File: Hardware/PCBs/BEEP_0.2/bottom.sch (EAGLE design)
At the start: 35 parts, among them IC1 74HCT00D, IC2 TCS32X0, Q2 IRLML2244, Q5 IRLML2244, Q6 IRLML2244, Q8 IRLML2244

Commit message: add simulation for comperator with hysteresis add library with atmel products (by element14) continue work on bottom shematic
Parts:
- removed 5V, GND, I1, I2, I3, I4, O1, O2, O3, O4: PTR1TP11SQ, testpad:PTR1TP11SQ
- removed LED1, LED2, LED3: (no value), led:LED3MM
- added C2, C3: 100n, rcl:C-EUC0805
- added D1, D2, D3, D4: CNY70, BEEP:CNY70
- added D5: (no value), diode:ZENER-DIODESMB
- added IC3, IC4: TCS32X0, BEEP:TCS32X0
- added Q1: DMN2075U, BEEP:DMN2075U
- added R12, R13, R14, R15, R16, R17, R18, R19, R20, R21, R22, R23, R24, R25, R26, R27, R28, R29, R30, R31, R32, R33, R34, R35, R36: (no value), rcl:R-EU_M0805
- added S1: (no value), switch-omron:40-XX
- added U1: LM239AMDREP, Texas Instruments_By_element14_Batch_1:LM239AMDREP
- added U2: ATTINY10-TSHR, Atmel_By_element14_Batch_1:ATTINY10-TSHR
- JP1: device pinhead:PINHD-2X5 -> pinhead:PINHD-2X3
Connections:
- removed net GND1: C1.1, IC2.GND, JP1.10, JP1.2, LED1.C, LED2.C, LED3.C, LED4.C, LED5.C, LED6.C
- removed net N$10: I3.TP, IC1C.I0, IC1C.I1
- removed net N$11: I4.TP, IC1D.I0, IC1D.I1
- removed net N$12: O4.TP, R8.2
- removed net N$16: O1.TP, R5.2
- removed net N$20: IC2.S0, JP1.8
- removed net N$21: IC2.S3, JP1.7
- removed net N$22: IC2.NOE, JP1.4
- removed net N$23: IC2.S1, JP1.6
- removed net N$24: C1.2, IC2.VDD, JP1.1
- removed net N$25: IC2.OUT, JP1.3
- removed net N$26: IC2.S2, JP1.5
- removed net N$27: JP1.9, R10.2, R11.2, R9.2
- removed net N$6: O2.TP, R6.2
- removed net N$7: I1.TP, IC1A.I0, IC1A.I1
- removed net N$8: I2.TP, IC1B.I0, IC1B.I1
- removed net N$9: O3.TP, R7.2
- new net +3V3: C1.2, C2.2, C3.2, D1.LED_A, D2.LED_A, D3.LED_A, D4.LED_A, IC2.S0, IC2.S1, IC2.VDD, IC3.S0, IC3.S1, IC3.VDD, IC4.S0, IC4.S1, IC4.VDD, R20.2, R21.2, R22.2, R23.2, R24.2, U1.VCC
- new net +7V: D5.C, R35.2
- new net BATT_GND: JP1.6, Q1.D, S1.S, S1.S1, U2.GND
- new net COLOR_1_NOE: IC2.NOE
- new net COLOR_2_NOE: IC3.NOE
- new net COLOR_3_NOE: IC4.NOE
- new net COMM_COLOR_F_OUT: IC2.OUT, IC3.OUT, IC4.OUT
- new net COMM_COLOR_S2: IC2.S2, IC3.S2, IC4.S2
- new net COMM_COLOR_S3: IC2.S3, IC3.S3, IC4.S3
- new net ENC_L1: R20.1, R30.1, U1.1OUT
- new net ENC_L1_RAW: D1.T_E, R13.2, R26.2
- new net ENC_L2: R21.1, R31.1, U1.2OUT
- new net ENC_L2_RAW: D2.T_E, R15.2, R27.2
- new net ENC_R1: R22.1, R32.1, U1.OUT3
- new net ENC_R1_RAW: D3.T_E, R17.2, R28.2
- new net ENC_R2: R23.1, R33.1, U1.OUT4
- new net ENC_R2_RAW: D4.T_E, R19.2, R29.2
- new net N$43: D1.LED_C, R12.2
- new net N$44: R26.1, R30.2, U1.1IN+
- new net N$45: R27.1, R31.2, U1.2IN+
- new net N$46: D2.LED_C, R14.2
- new net N$47: R28.1, R32.2, U1.3IN+
- new net N$48: D3.LED_C, R16.2
- new net N$49: R29.1, R33.2, U1.4IN+
- new net N$50: D4.LED_C, R18.2
- new net PWM_IN1: IC1A.I0, IC1A.I1
- new net PWM_IN2: IC1B.I0, IC1B.I1
- new net PWM_IN3: IC1C.I0, IC1C.I1
- new net PWM_IN4: IC1D.I0, IC1D.I1
- new net PWM_OUT1: R5.2
- new net PWM_OUT2: R6.2
- new net PWM_OUT3: R7.2
- new net PWM_OUT4: R8.2
- new net RESET: JP1.5, R36.1, U2.PB3
- new net SWITCHED_GROUND: Q1.S
- new net TINY_VCC: D5.A, JP1.2, R36.2, U2.VCC
- new net TPICLK: JP1.3, R34.2, R35.1, S1.P, S1.P1, U2.PB1, U2.PB2
- new net TPIDATA: JP1.1, Q1.G, U2.PB0
- new net U_REF: R24.1, R25.2, U1.1IN-, U1.2IN-, U1.3IN-, U1.4IN-
- net +5V: now also D1.T_C, D2.T_C, D3.T_C, D4.T_C, R10.2, R11.2, R9.2; no longer 5V.TP
- net GND: now also C1.1, C2.1, C3.1, IC1P.GND, IC2.GND, IC3.GND, IC4.GND, LED4.C, LED5.C, LED6.C, R12.1, R13.1, R14.1, R15.1, R16.1, R17.1, R18.1, R19.1, R25.1, R34.1, U1.GND; no longer GND.TP
- net N$17: no longer LED2.A
- net N$18: no longer LED1.A
- net N$19: no longer LED3.A
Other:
- moved on the sheet: C1, IC2, LED4, LED5, LED6, R10, R11, R9

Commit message: add more distance boards continue work on bottom pcb
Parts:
- added JP2: (no value), pinhead:PINHD-1X5
- added JP3: (no value), pinhead:PINHD-2X4
- added JP4: (no value), pinhead:PINHD-1X3
- added X1: (no value), con-ftop-orientation-hole:FTOP-10
- S1: device switch-omron:40-XX -> switch-omron:10-XX
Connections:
- removed net COLOR_1_NOE: IC2.NOE
- removed net COLOR_2_NOE: IC3.NOE
- removed net COLOR_3_NOE: IC4.NOE
- removed net COMM_COLOR_F_OUT: IC2.OUT, IC3.OUT, IC4.OUT
- removed net COMM_COLOR_S2: IC2.S2, IC3.S2, IC4.S2
- removed net COMM_COLOR_S3: IC2.S3, IC3.S3, IC4.S3
- removed net SWITCHED_GROUND: Q1.S
- new net COLOR_DIODE_1: IC2.S2, IC3.S2, IC4.S2, X1-4.1
- new net COLOR_DIODE_2: IC2.S3, IC3.S3, IC4.S3, X1-3.1
- new net COLOR_FREQ_OUT: IC2.OUT, IC3.OUT, IC4.OUT, X1-7.1
- new net COLOR_SENSOR_1: IC2.NOE, X1-2.1
- new net COLOR_SENSOR_2: IC3.NOE, X1-6.1
- new net COLOR_SENSOR_3: IC4.NOE, X1-5.1
- new net COLOR_SENSOR_PWM_LED: R10.2, R11.2, R9.2, X1-9.1
- new net N$6: S1.P, S1.P1, U2.PB2
- new net SWITCHED_GND: JP4.2, Q1.S
- net +3V3: now also X1-10.1
- net +5V: now also JP2.5; no longer R10.2, R11.2, R9.2
- net +7V: now also JP4.3
- net BATT_GND: now also JP4.1
- net ENC_L1: now also JP2.1
- net ENC_L2: now also JP2.2
- net ENC_R1: now also JP2.3
- net ENC_R2: now also JP2.4
- net GND: now also X1-8.1
- net PWM_IN1: now also JP3.1
- net PWM_IN2: now also JP3.3
- net PWM_IN3: now also JP3.5
- net PWM_IN4: now also JP3.7
- net PWM_OUT1: now also JP3.2
- net PWM_OUT2: now also JP3.4
- net PWM_OUT3: now also JP3.6
- net PWM_OUT4: now also JP3.8
- net TPICLK: no longer S1.P, S1.P1, U2.PB2
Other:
- moved on the sheet: R20, R21, R22, R23

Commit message: continue work on bottom pcb
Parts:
- R12: device rcl:R-EU_M0805 -> rcl:R-EU_R0805
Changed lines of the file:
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@@
 <part name="D1" library="BEEP" deviceset="CNY70" device=""/>
 <part name="GND6" library="supply1" deviceset="GND" device=""/>
-<part name="R12" library="rcl" deviceset="R-EU_" device="M0805"/>
+<part name="R12" library="rcl" deviceset="R-EU_" device="R0805"/>
 <part name="R13" library="rcl" deviceset="R-EU_" device="M0805"/>
 <part name="GND7" library="supply1" deviceset="GND" device=""/>

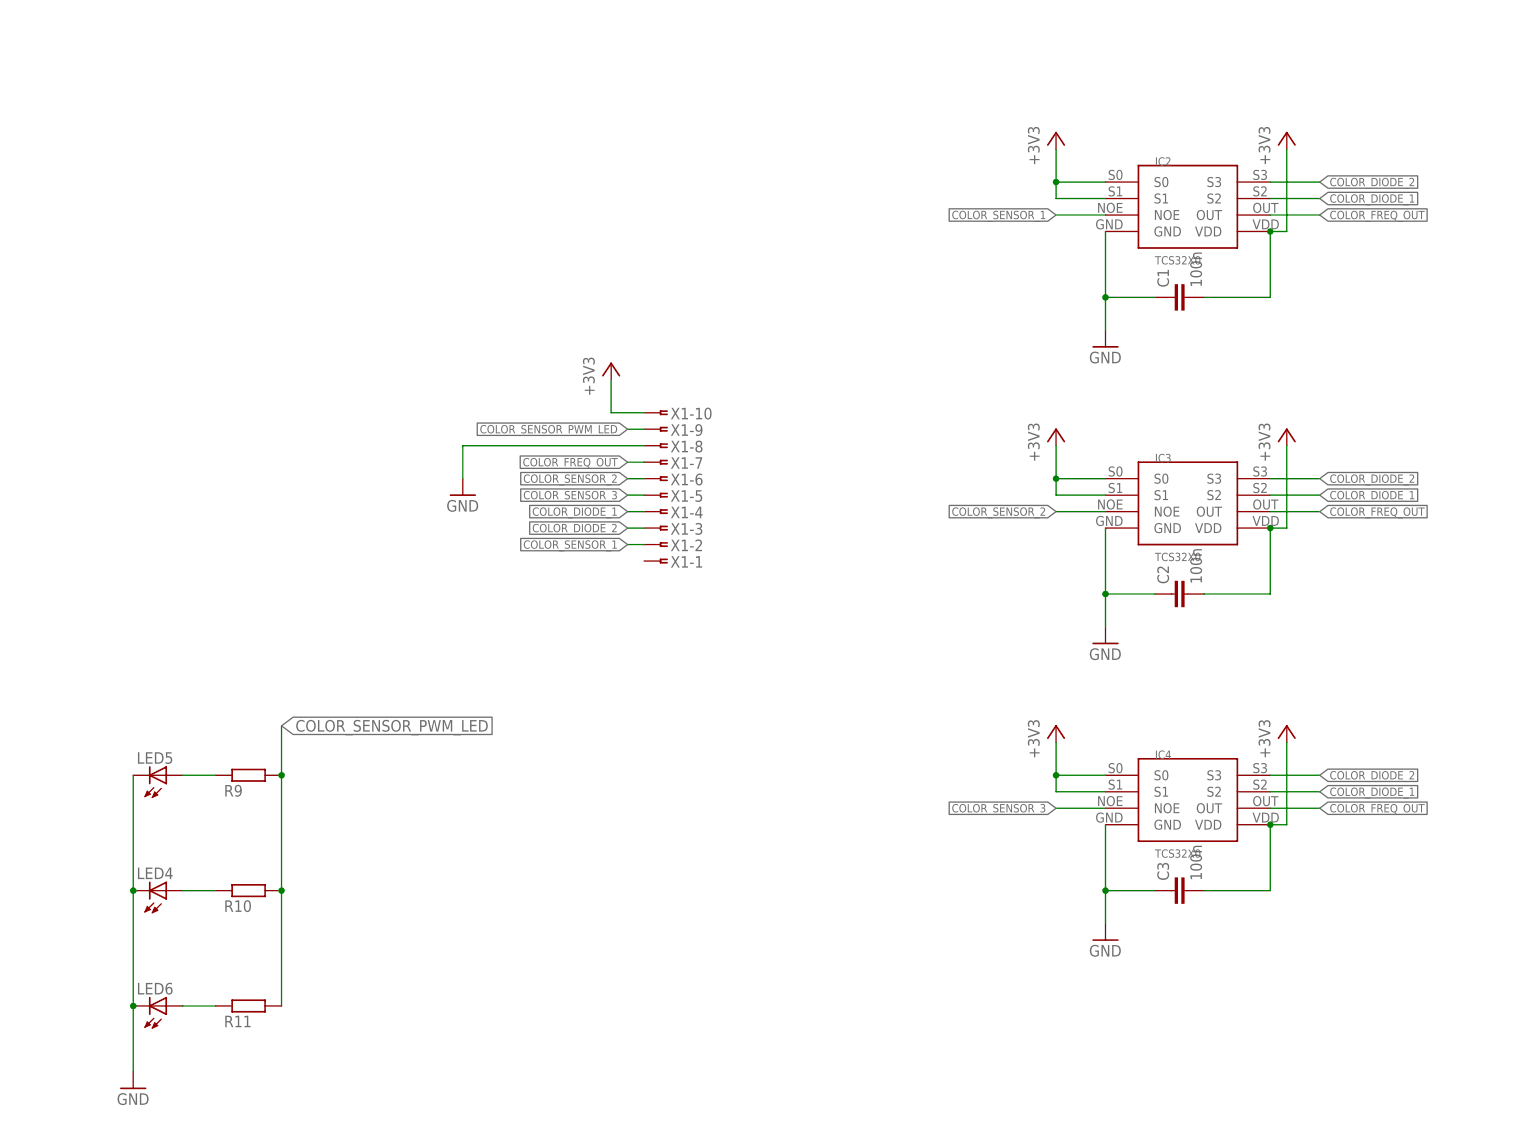
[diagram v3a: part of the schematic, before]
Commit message: continue work on bottom pcb
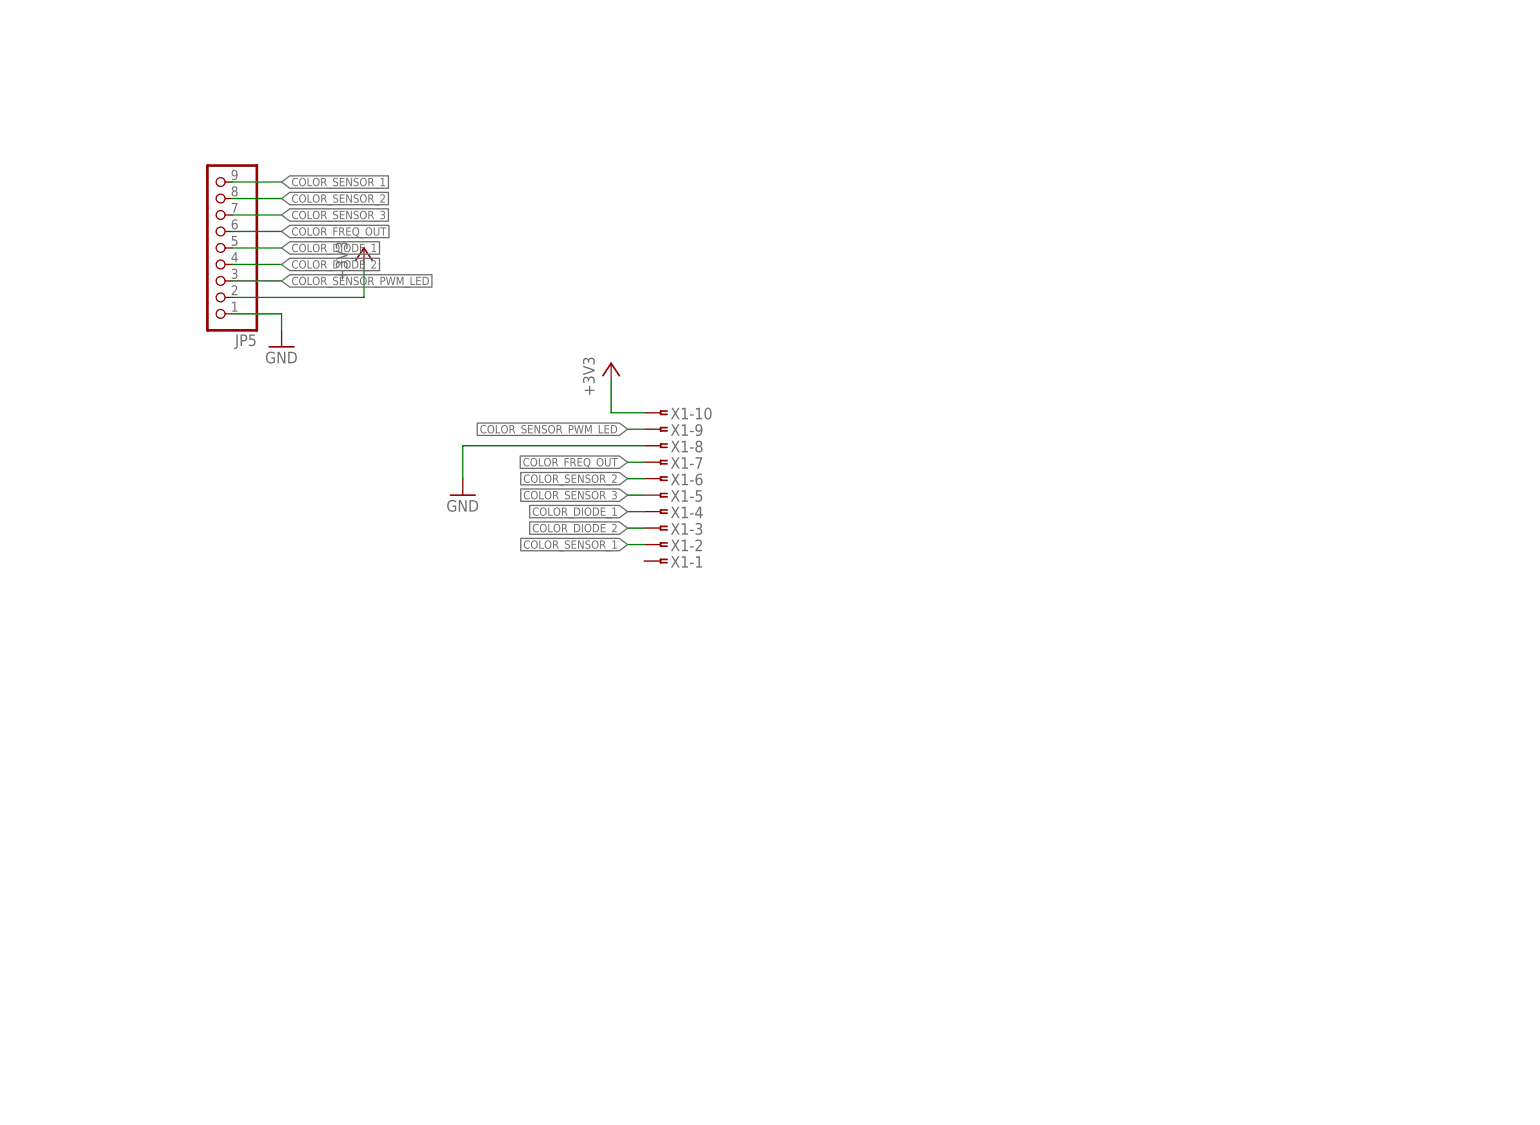
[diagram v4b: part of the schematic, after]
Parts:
- removed C1, C2, C3: 100n, rcl:C-EUC0805
- removed IC2, IC3, IC4: TCS32X0, BEEP:TCS32X0
- removed LED4, LED5, LED6: NFSG036BT, led:NFSG036BT
- removed R10, R11, R9: (no value), rcl:R-EU_M0805
- added JP5: (no value), pinhead:PINHD-1X9
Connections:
- removed net N$17: LED5.A, R9.1
- removed net N$18: LED4.A, R10.1
- removed net N$19: LED6.A, R11.1
- net +3V3: now also JP5.2; no longer C1.2, C2.2, C3.2, IC2.S0, IC2.S1, IC2.VDD, IC3.S0, IC3.S1, IC3.VDD, IC4.S0, IC4.S1, IC4.VDD
- net COLOR_DIODE_1: now also JP5.5; no longer IC2.S2, IC3.S2, IC4.S2
- net COLOR_DIODE_2: now also JP5.4; no longer IC2.S3, IC3.S3, IC4.S3
- net COLOR_FREQ_OUT: now also JP5.6; no longer IC2.OUT, IC3.OUT, IC4.OUT
- net COLOR_SENSOR_1: now also JP5.9; no longer IC2.NOE
- net COLOR_SENSOR_2: now also JP5.8; no longer IC3.NOE
- net COLOR_SENSOR_3: now also JP5.7; no longer IC4.NOE
- net COLOR_SENSOR_PWM_LED: now also JP5.3; no longer R10.2, R11.2, R9.2
- net GND: now also JP5.1; no longer C1.1, C2.1, C3.1, IC2.GND, IC3.GND, IC4.GND, LED4.C, LED5.C, LED6.C

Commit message: continue work on bottom pcbs
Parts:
- JP4: device pinhead:PINHD-1X3 -> pinhead:PINHD-1X4
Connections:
- net +7V: now also JP4.4
- net BATT_GND: now also JP4.2; no longer JP4.1
- net PWM_IN1: now also JP3.2; no longer JP3.1
- net PWM_IN2: now also JP3.4; no longer JP3.3
- net PWM_IN3: now also JP3.6; no longer JP3.5
- net PWM_IN4: now also JP3.8; no longer JP3.7
- net PWM_OUT1: now also JP3.1; no longer JP3.2
- net PWM_OUT2: now also JP3.3; no longer JP3.4
- net PWM_OUT3: now also JP3.5; no longer JP3.6
- net PWM_OUT4: now also JP3.7; no longer JP3.8
- net SWITCHED_GND: now also JP4.1; no longer JP4.2
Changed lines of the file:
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@@
 <part name="JP2" library="pinhead" deviceset="PINHD-1X5" device=""/>
 <part name="JP3" library="pinhead" deviceset="PINHD-2X4" device=""/>
-<part name="JP4" library="pinhead" deviceset="PINHD-1X3" device=""/>
+<part name="JP4" library="pinhead" deviceset="PINHD-1X4" device=""/>
 <part name="SUPPLY3" library="supply2" deviceset="+7V" device=""/>
 <part name="P+2" library="supply1" deviceset="+5V" device=""/>
@@
 <instance part="JP2" gate="A" x="502.92" y="276.86"/>
 <instance part="JP3" gate="A" x="66.04" y="35.56"/>
-<instance part="JP4" gate="A" x="203.2" y="243.84"/>
+<instance part="JP4" gate="A" x="203.2" y="241.3"/>
 <instance part="SUPPLY3" gate="G$1" x="167.64" y="243.84"/>
 <instance part="P+2" gate="1" x="480.06" y="276.86" rot="MR0"/>
@@
 </segment>
 <segment>
-<pinref part="JP3" gate="A" pin="4"/>
-<wire x1="71.12" y1="38.1" x2="78.74" y2="38.1" width="0.1524" layer="91"/>
-<label x="78.74" y="38.1" size="1.27" layer="95" xref="yes"/>
+<pinref part="JP3" gate="A" pin="3"/>
+<wire x1="63.5" y1="38.1" x2="55.88" y2="38.1" width="0.1524" layer="91"/>
+<label x="55.88" y="38.1" size="1.27" layer="95" rot="R180" xref="yes"/>
 </segment>
 </net>
@@
 </segment>
 <segment>
-<pinref part="JP3" gate="A" pin="6"/>
-<wire x1="71.12" y1="35.56" x2="78.74" y2="35.56" width="0.1524" layer="91"/>
-<label x="78.74" y="35.56" size="1.27" layer="95" xref="yes"/>
+<pinref part="JP3" gate="A" pin="5"/>
+<wire x1="63.5" y1="35.56" x2="55.88" y2="35.56" width="0.1524" layer="91"/>
+<label x="55.88" y="35.56" size="1.27" layer="95" rot="R180" xref="yes"/>
 </segment>
 </net>
@@
 </segment>
 <segment>
-<pinref part="JP3" gate="A" pin="8"/>
-<wire x1="71.12" y1="33.02" x2="78.74" y2="33.02" width="0.1524" layer="91"/>
-<label x="78.74" y="33.02" size="1.27" layer="95" xref="yes"/>
+<pinref part="JP3" gate="A" pin="7"/>
+<wire x1="63.5" y1="33.02" x2="55.88" y2="33.02" width="0.1524" layer="91"/>
+<label x="55.88" y="33.02" size="1.27" layer="95" rot="R180" xref="yes"/>
 </segment>
 </net>
@@
 </segment>
 <segment>
-<pinref part="JP3" gate="A" pin="2"/>
-<wire x1="71.12" y1="40.64" x2="78.74" y2="40.64" width="0.1524" layer="91"/>
-<label x="78.74" y="40.64" size="1.27" layer="95" xref="yes"/>
+<pinref part="JP3" gate="A" pin="1"/>
+<wire x1="63.5" y1="40.64" x2="55.88" y2="40.64" width="0.1524" layer="91"/>
+<label x="55.88" y="40.64" size="1.27" layer="95" rot="R180" xref="yes"/>
 </segment>
 </net>
@@
 </segment>
 <segment>
-<pinref part="JP3" gate="A" pin="1"/>
-<wire x1="63.5" y1="40.64" x2="55.88" y2="40.64" width="0.1524" layer="91"/>
-<label x="55.88" y="40.64" size="1.27" layer="95" rot="R180" xref="yes"/>
+<pinref part="JP3" gate="A" pin="2"/>
+<wire x1="71.12" y1="40.64" x2="78.74" y2="40.64" width="0.1524" layer="91"/>
+<label x="78.74" y="40.64" size="1.27" layer="95" xref="yes"/>
 </segment>
 </net>
@@
 </segment>
 <segment>
-<pinref part="JP3" gate="A" pin="3"/>
-<wire x1="63.5" y1="38.1" x2="55.88" y2="38.1" width="0.1524" layer="91"/>
-<label x="55.88" y="38.1" size="1.27" layer="95" rot="R180" xref="yes"/>
+<pinref part="JP3" gate="A" pin="4"/>
+<wire x1="71.12" y1="38.1" x2="78.74" y2="38.1" width="0.1524" layer="91"/>
+<label x="78.74" y="38.1" size="1.27" layer="95" xref="yes"/>
 </segment>
 </net>
@@
 </segment>
 <segment>
-<pinref part="JP3" gate="A" pin="5"/>
-<wire x1="63.5" y1="35.56" x2="55.88" y2="35.56" width="0.1524" layer="91"/>
-<label x="55.88" y="35.56" size="1.27" layer="95" rot="R180" xref="yes"/>
+<pinref part="JP3" gate="A" pin="6"/>
+<wire x1="71.12" y1="35.56" x2="78.74" y2="35.56" width="0.1524" layer="91"/>
+<label x="78.74" y="35.56" size="1.27" layer="95" xref="yes"/>
 </segment>
 </net>
@@
 </segment>
 <segment>
-<pinref part="JP3" gate="A" pin="7"/>
-<wire x1="63.5" y1="33.02" x2="55.88" y2="33.02" width="0.1524" layer="91"/>
-<label x="55.88" y="33.02" size="1.27" layer="95" rot="R180" xref="yes"/>
+<pinref part="JP3" gate="A" pin="8"/>
+<wire x1="71.12" y1="33.02" x2="78.74" y2="33.02" width="0.1524" layer="91"/>
+<label x="78.74" y="33.02" size="1.27" layer="95" xref="yes"/>
 </segment>
 </net>
@@
 <pinref part="JP4" gate="A" pin="3"/>
 <pinref part="SUPPLY3" gate="G$1" pin="+7V"/>
-<wire x1="200.66" y1="241.3" x2="167.64" y2="241.3" width="0.1524" layer="91"/>
+<wire x1="200.66" y1="241.3" x2="193.04" y2="241.3" width="0.1524" layer="91"/>
+<pinref part="JP4" gate="A" pin="4"/>
+<wire x1="193.04" y1="241.3" x2="167.64" y2="241.3" width="0.1524" layer="91"/>
+<wire x1="200.66" y1="238.76" x2="193.04" y2="238.76" width="0.1524" layer="91"/>
+<wire x1="193.04" y1="238.76" x2="193.04" y2="241.3" width="0.1524" layer="91"/>
+<junction x="193.04" y="241.3"/>
 </segment>
 </net>
@@
 </segment>
 <segment>
-<pinref part="JP4" gate="A" pin="1"/>
-<wire x1="200.66" y1="246.38" x2="193.04" y2="246.38" width="0.1524" layer="91"/>
-<label x="193.04" y="246.38" size="1.27" layer="95" rot="R180" xref="yes"/>
+<pinref part="JP4" gate="A" pin="2"/>
+<wire x1="200.66" y1="243.84" x2="193.04" y2="243.84" width="0.1524" layer="91"/>
+<label x="193.04" y="243.84" size="1.27" layer="95" rot="R180" xref="yes"/>
 </segment>
 </net>
@@
 <net name="SWITCHED_GND" class="0">
 <segment>
-<pinref part="JP4" gate="A" pin="2"/>
-<wire x1="200.66" y1="243.84" x2="193.04" y2="243.84" width="0.1524" layer="91"/>
-<label x="193.04" y="243.84" size="1.27" layer="95" rot="R180" xref="yes"/>
-</segment>
-<segment>
 <wire x1="185.42" y1="317.5" x2="190.5" y2="317.5" width="0.1524" layer="91"/>
 <pinref part="Q1" gate="G$1" pin="S"/>
@@
 <label x="190.5" y="317.5" size="1.27" layer="95" xref="yes"/>
 </segment>
-</net>
+<segment>
+<pinref part="JP4" gate="A" pin="1"/>
+<wire x1="200.66" y1="246.38" x2="193.04" y2="246.38" width="0.1524" layer="91"/>
+<label x="193.04" y="246.38" size="1.27" layer="95" rot="R180" xref="yes"/>
+</segment>
+</net>

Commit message: continue work on bottom pcb
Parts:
- removed D5: (no value), diode:ZENER-DIODESMB
- added C1, C2, C3: (no value), rcl:C-EUC0603
- added R10: 100k, rcl:R-EU_M0805
- added R11: 1M, rcl:R-EU_M0805
- added R9: 10k, rcl:R-EU_M0805
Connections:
- removed net N$6: S1.P, S1.P1, U2.PB2
- new net PB0/TPIDATA: R9.1, U2.PB0
- new net PB1/TPICLK: Q1.G, R11.2, S1.S, S1.S1, U2.PB1
- new net PB2/SOFT_OFF: R10.1, R9.2, S1.P, S1.P1, U2.PB2
- net +3V3: now also C1.1, R10.2, R36.2, U2.VCC
- net +7V: no longer D5.C
- net BATT_GND: now also Q1.S, R11.1; no longer Q1.D, S1.S, S1.S1, U2.GND
- net GND: now also C1.2, U2.GND
- net RESET: now also R34.2, R35.1
- net SWITCHED_GND: now also Q1.D; no longer Q1.S
- net TINY_VCC: no longer D5.A, R36.2, U2.VCC
- net TPICLK: no longer R34.2, R35.1, U2.PB1
- net TPIDATA: no longer Q1.G, U2.PB0
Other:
- moved on the sheet: Q1, R34, R35, R36, S1
